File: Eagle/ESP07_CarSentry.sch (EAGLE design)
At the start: 43 parts, among them Q1 PFET, Q2 NPN/NFET, Q3 NPN/NFET, Q4 NPN

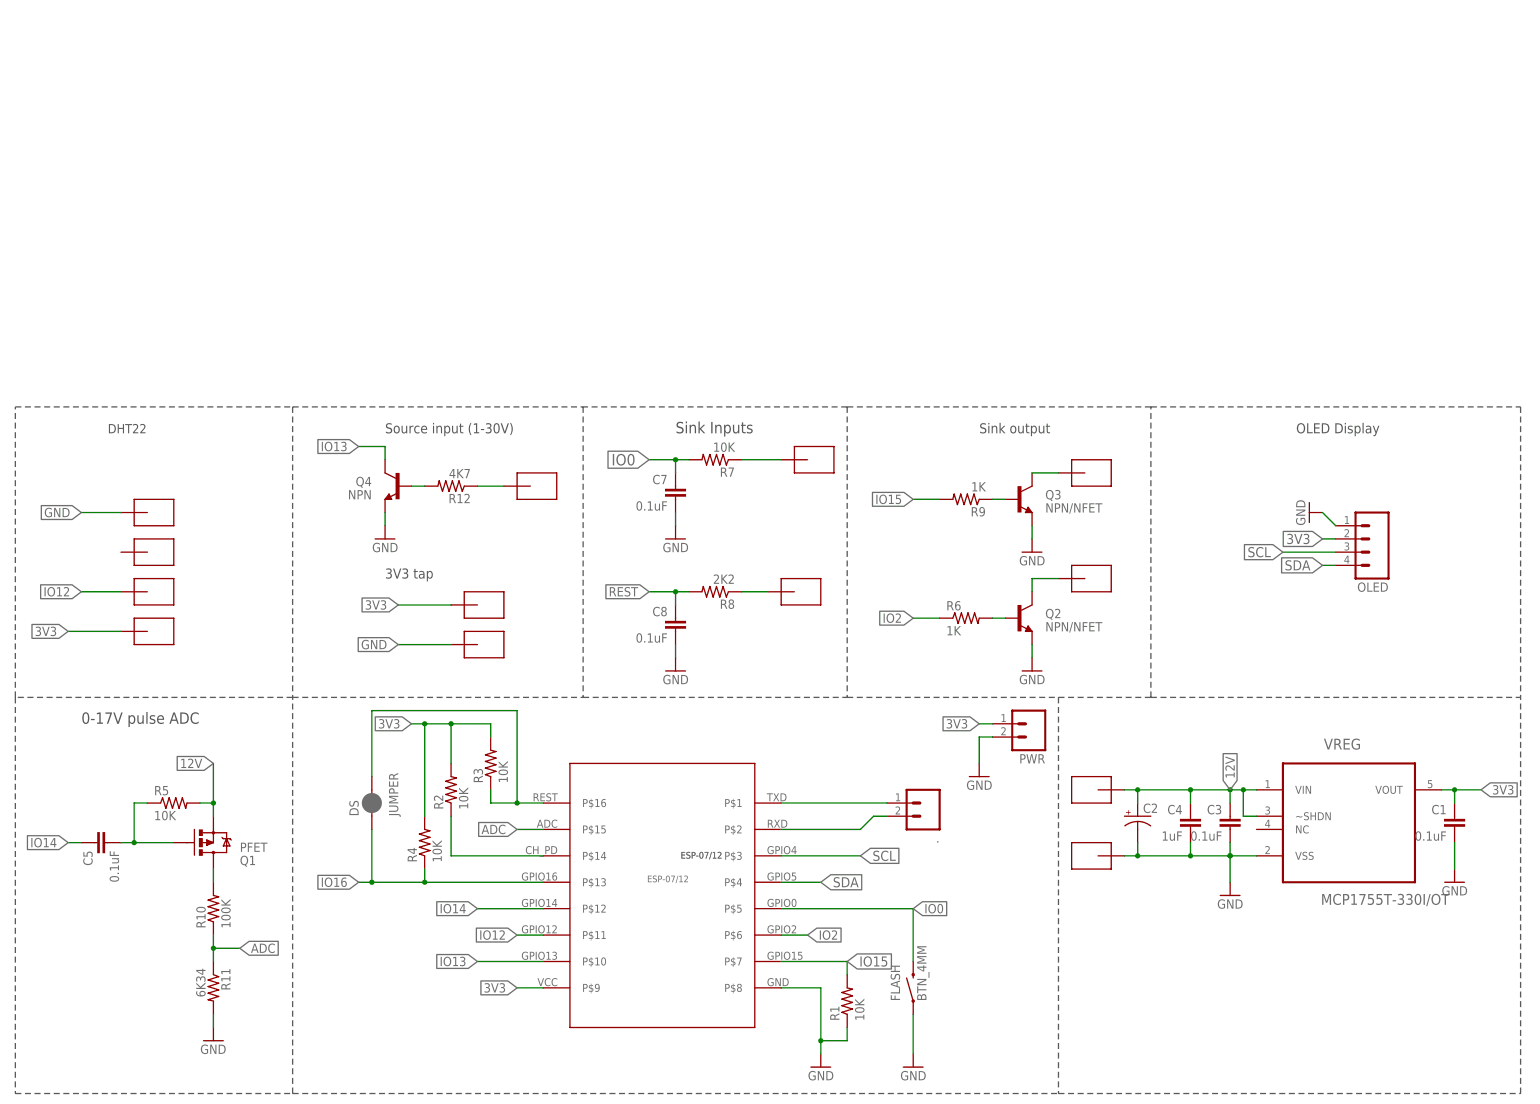
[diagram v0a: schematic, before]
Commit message: Switched Out 2 to PFET
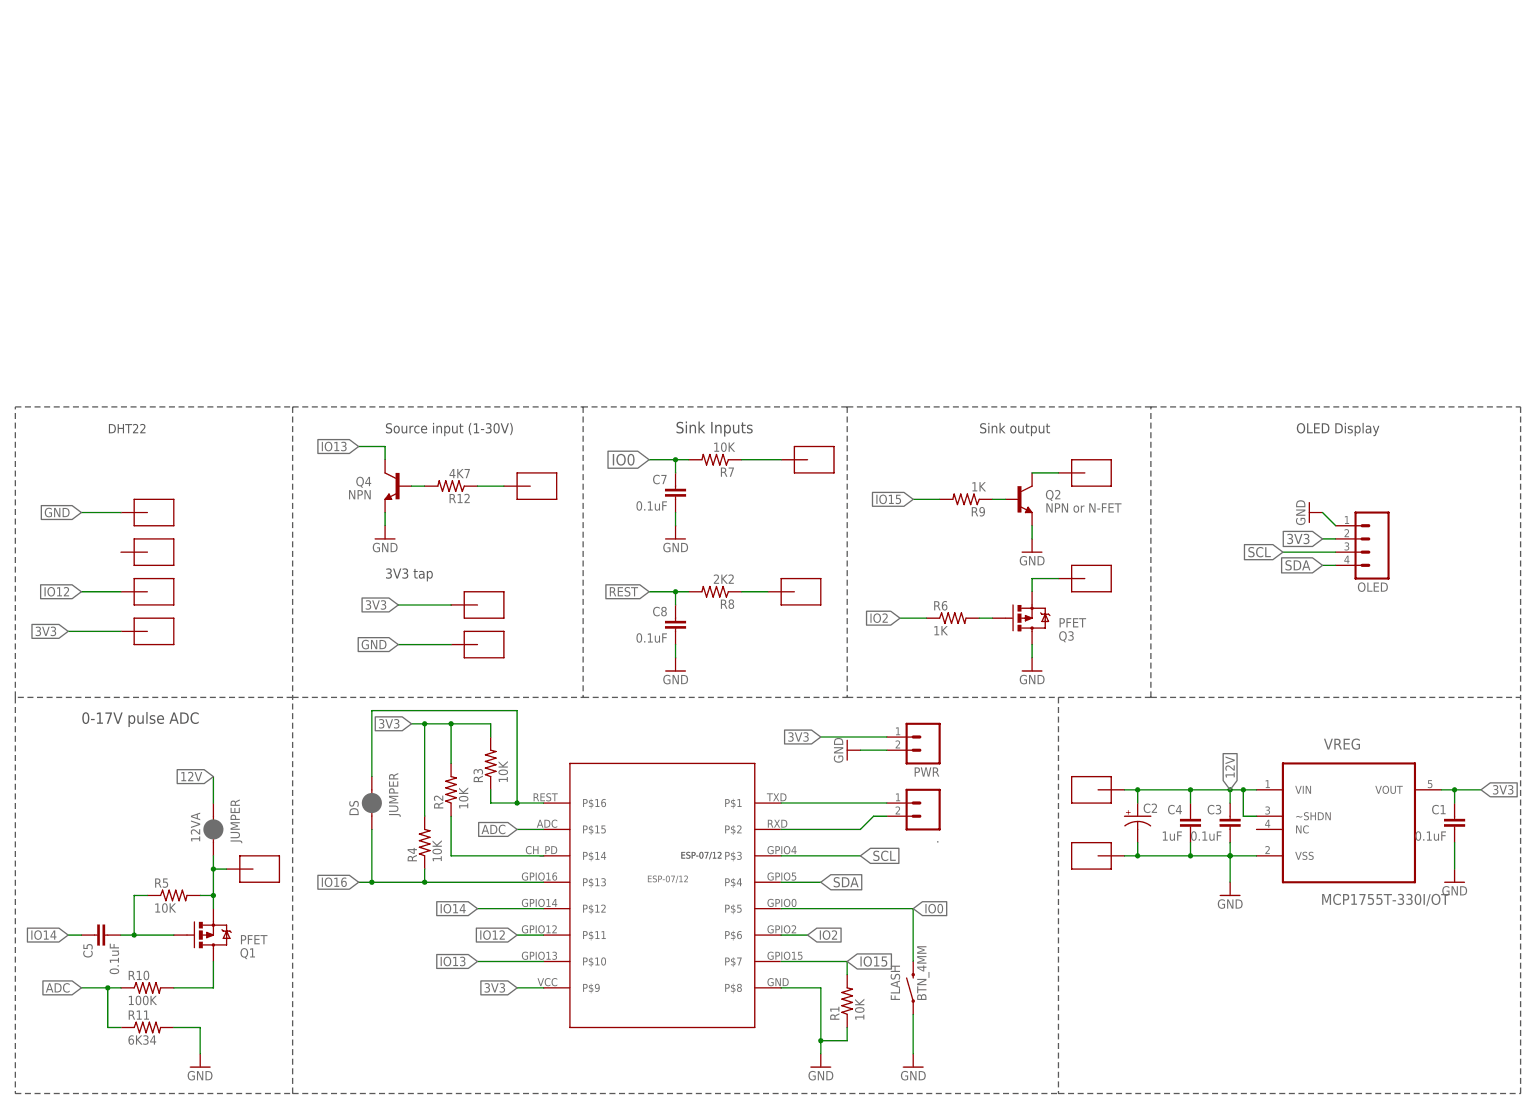
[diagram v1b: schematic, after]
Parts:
- added 12VA: JUMPER, SparkFun-Passives:JUMPER-PAD-2-NC_BY_PASTE
- added U$13: SMD-PAD1, CuriousTech:SMD-PAD1
- Q2: value NPN/NFET -> NPN or N-FET
- Q3: value NPN/NFET -> PFET; device SparkFun-DiscreteSemi:TRANSISTOR_NPNSOT23-3 -> SparkFun-DiscreteSemi:MOSFET-PCHANNEL
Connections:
- new net ADCHI: 12VA.1, Q1.S, R5.2, U$13.P$1
- net 12V: now also 12VA.2; no longer Q1.S, R5.2
- net GND: now also Q3.D; no longer Q3.E
- net N$2: now also Q3.G; no longer Q2.B
- net N$4: now also Q3.S; no longer Q2.C
- net N$6: now also Q2.B; no longer Q3.B
- net N$7: now also Q2.C; no longer Q3.C
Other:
- moved on the sheet: C5, PWR, Q1, Q2, R10, R11, R5, R6

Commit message: rev 3
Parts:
- removed C2: (no value), SparkFun-Capacitors:CAP_POLPTH1
- removed C3: 0.1uF, SparkFun-Capacitors:CAP
- removed PWR: (no value), SparkFun-Connectors:M02PTH
- removed VREG: MCP1755T-330I/OT, Microchip_By_element14_Batch_1:MCP1802T-3002I/OT
- added C11, C6, C9: 0.1uF, SparkFun-Capacitors:CAP
- added D5: BAT20J, SparkFun-DiscreteSemi:DIODE-SCHOTTKY-BAT20J
- added L1, L2: (no value), SparkFun-Passives:INDUCTOR0805
- added Q5: NPN, SparkFun-DiscreteSemi:TRANSISTOR_NPNSOT23-3
- added Q6: PFET, SparkFun-DiscreteSemi:MOSFET-PCHANNEL
- added R13: 4K7, SparkFun-Resistors:RESISTOR0805-RES
- added R14: 1K, SparkFun-Resistors:RESISTOR0805-RES
- added VREG1: LMR16006YQ3DDCRQ1, CuriousTech:LMR16006YQ
- C1: value 0.1uF -> 2.2uF
- C4: value 1uF -> 10uF
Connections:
- removed net 12V: 12VA.2, C2.+, C3.1, C4.1, U$16.P$1, VREG.VIN, VREG.~SHDN
- new net +12V: 12VA.2, C1.1, C6.1, U$16.P$1, VREG1.VIN
- new net N$12: Q5.B, R13.2
- new net N$13: C11.1, D5.C, L1.1, L2.1, VREG1.SW
- new net N$14: C11.2, VREG1.CB
- new net N$15: R13.1, U$10.P$1
- new net N$16: Q6.S, U$13.P$1
- new net N$17: Q6.G, R14.2
- net 3V3: now also C4.1, C9.1, L1.2, L2.2, VREG1.FB; no longer C1.1, PWR.1, U$10.P$1, VREG.VOUT
- net ADCHI: no longer U$13.P$1
- net GND: now also C6.2, C9.2, D5.A, Q5.E, Q6.D, VREG1.GND; no longer C2.-, C3.2, PWR.2, VREG.VSS
- net RXD: now also Q5.C
- net TXD: now also R14.1
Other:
- note added: "Switching supply"
- note removed: "3V3 tap"
- moved on the sheet: 12VA, C1, C4, C5, C7, C8, OLED, Q1, Q2, Q3, Q4, R10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
